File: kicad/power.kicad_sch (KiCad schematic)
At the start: 66 parts, among them J1 USB_C_Receptacle_USB2.0_14P, SW1 SW_Push, SW2 SW_Push, U1 TPS628438DRL, U2 BQ25895RTW, U3 USBLC6-2SC6, U4 MAX17263xxTE, U5 TLV70233_SOT23-5, U6 TPS7A4701xRGW

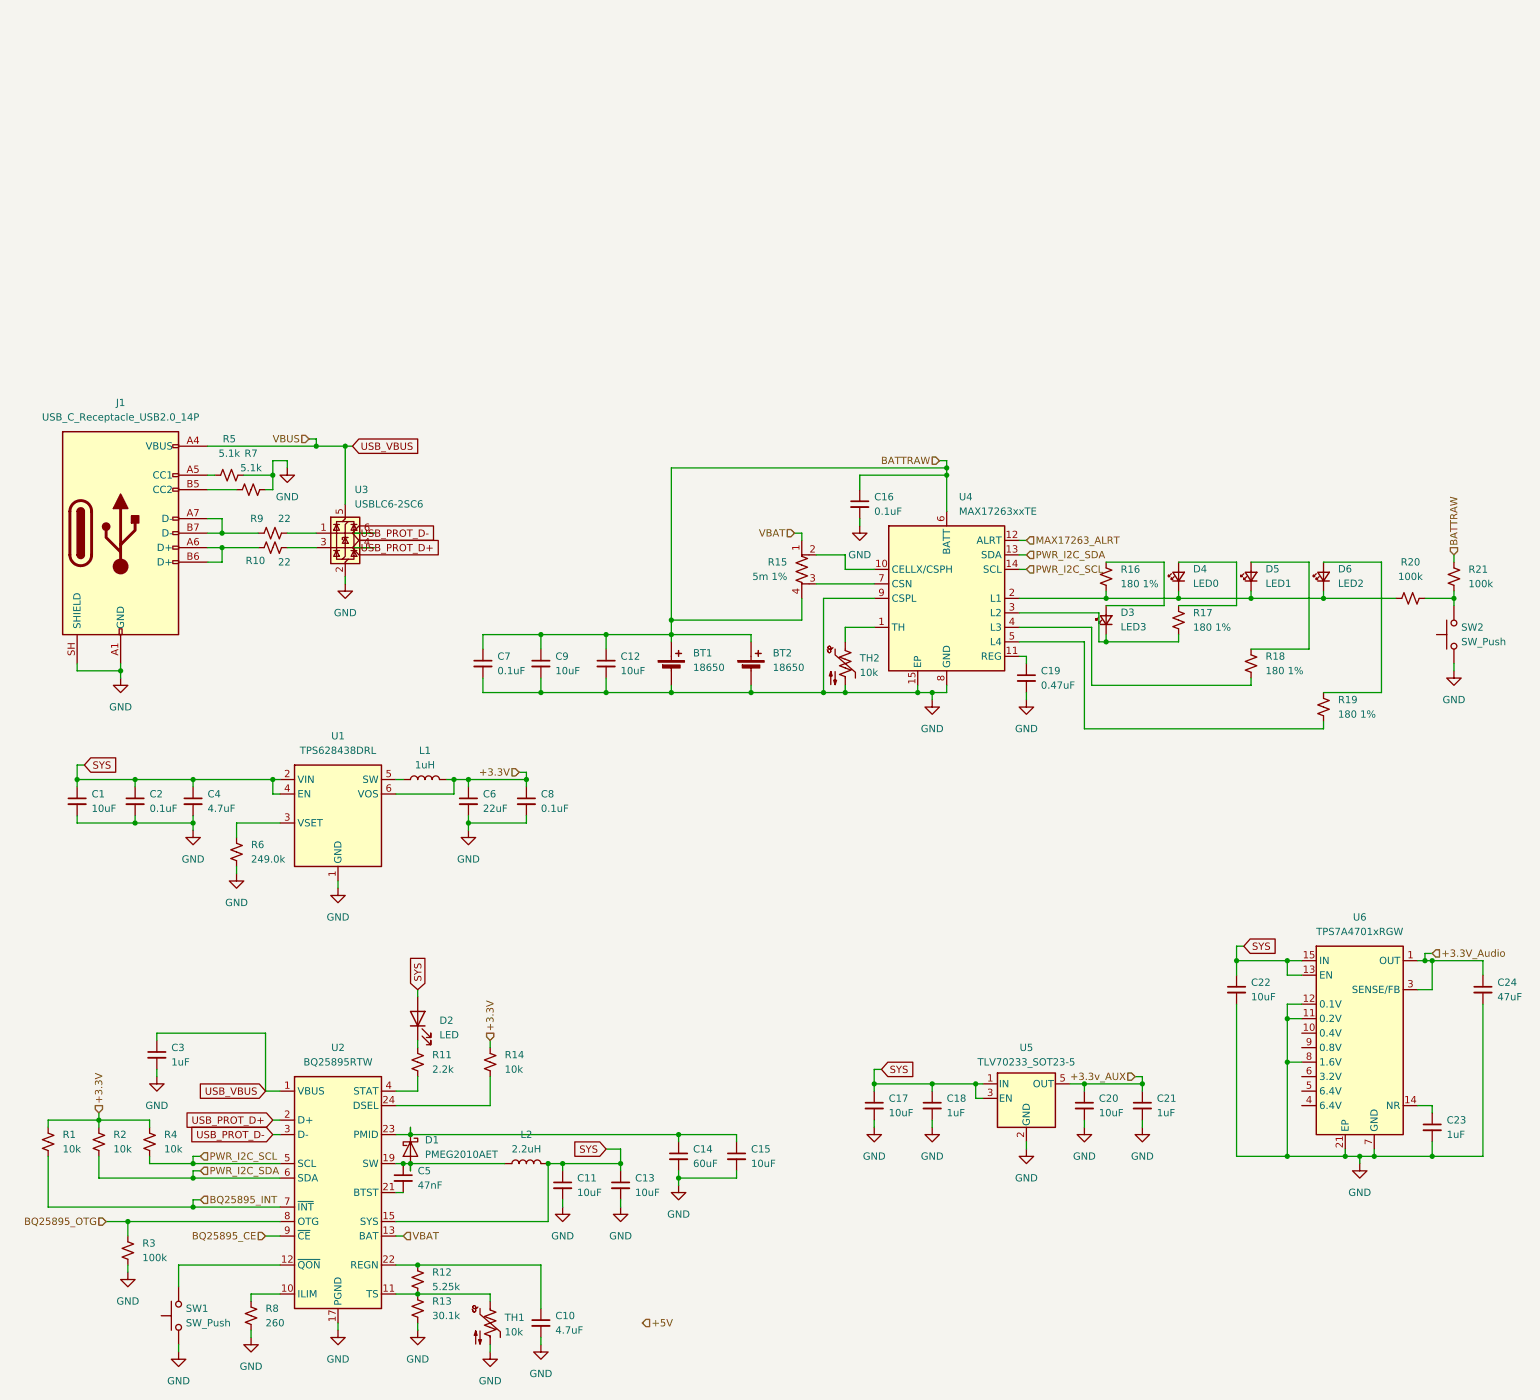
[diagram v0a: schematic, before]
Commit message: add PMM instead of poewr stage
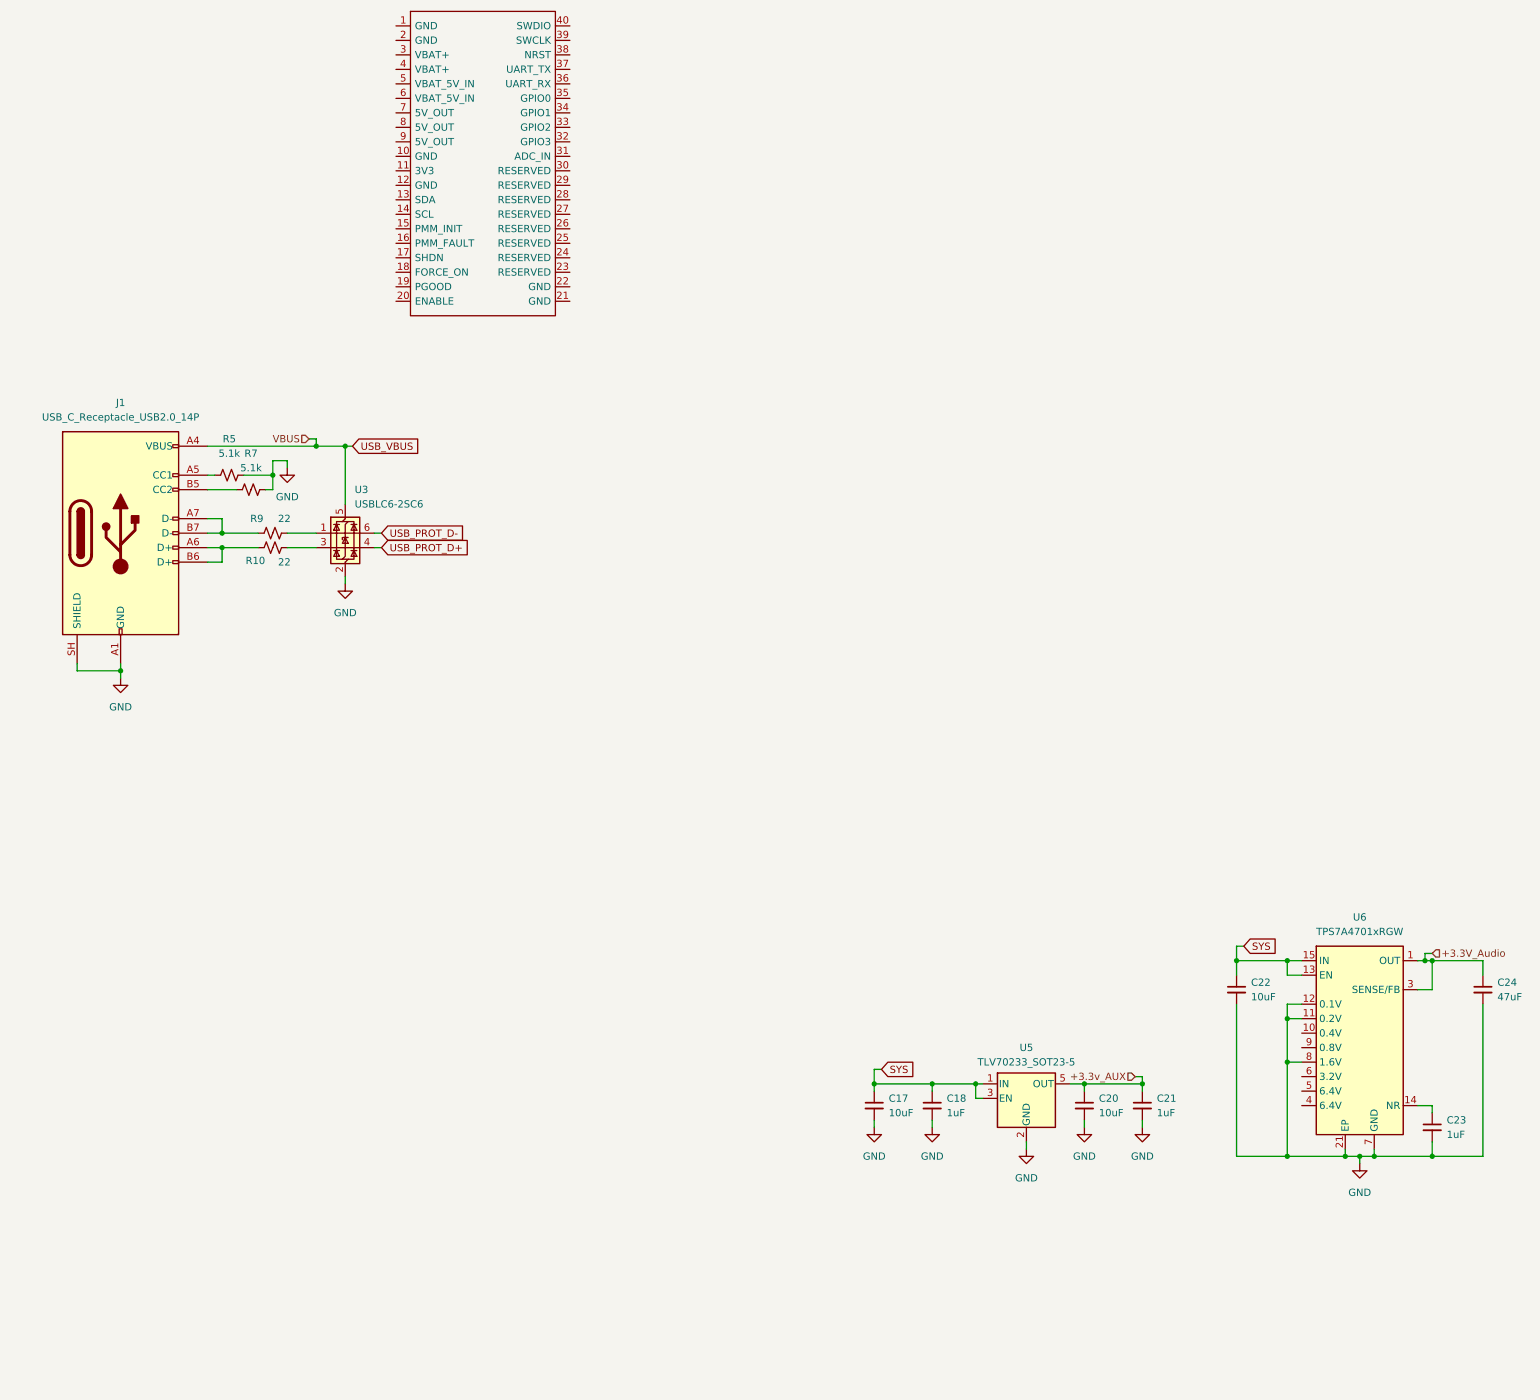
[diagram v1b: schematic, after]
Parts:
- removed BT1, BT2: 18650, Battery:BatteryHolder_Keystone_1042_1x18650, symbol Device:Battery_Cell
- removed C1, C11, C12, C13, C15, C9: 10uF, symbol Device:C_Small
- removed C10, C4: 4.7uF, symbol Device:C_Small
- removed C14: 60uF, symbol Device:C_Small
- removed C16, C2, C7, C8: 0.1uF, symbol Device:C_Small
- removed C19: 0.47uF, symbol Device:C_Small
- removed C3: 1uF, symbol Device:C_Small
- removed C5: 47nF, symbol Device:C_Small
- removed C6: 22uF, symbol Device:C_Small
- removed D1: PMEG2010AET, Package_TO_SOT_SMD:SOT-23, symbol Diode:PMEG2010AET
- removed D2: LED, symbol Device:LED
- removed D3: LED3, symbol Device:LED_Small
- removed D4: LED0, symbol Device:LED_Small
- removed D5: LED1, symbol Device:LED_Small
- removed D6: LED2, symbol Device:LED_Small
- removed L1: 1uH, symbol Device:L
- removed L2: 2.2uH, symbol Device:L
- removed R1, R14, R2, R4: 10k, symbol Device:R_Small_US
- removed R11: 2.2k, symbol Device:R_Small_US
- removed R12: 5.25k, symbol Device:R_Small_US
- removed R13: 30.1k, symbol Device:R_Small_US
- removed R15: 5m 1%, symbol Device:R_Shunt_US
- removed R16, R17, R18, R19: 180 1%, symbol Device:R_Small_US
- removed R20, R21, R3: 100k, symbol Device:R_Small_US
- removed R6: 249.0k, symbol Device:R_Small_US
- removed R8: 260, symbol Device:R_Small_US
- removed SW1, SW2: SW_Push, symbol Switch:SW_Push
- removed TH1, TH2: 10k, symbol Device:Thermistor_NTC_US
- removed U1: TPS628438DRL, Package_TO_SOT_SMD:SOT-563, symbol Regulator_Switching:TPS628436DRL
- removed U2: BQ25895RTW, Package_DFN_QFN:Texas_RTW_WQFN-24-1EP_4x4mm_P0.5mm_EP2.7x2.7mm_ThermalVias, symbol Battery_Management:BQ25895RTW
- removed U4: MAX17263xxTE, Package_DFN_QFN:DFN-14-1EP_3x3mm_P0.4mm_EP1.78x2.35mm, symbol Battery_Management:MAX17263xxTE
- added A1: PMM, PMM:PMM, symbol PMM:PMM
